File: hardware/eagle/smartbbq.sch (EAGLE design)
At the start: 58 parts, among them J1 MJ_2523_SMT, J2 MJ_2523_SMT, J3 MJ_2523_SMT, J4 MJ_2523_SMT, J5 5.5od/2.1id, J6 5.5od/2.5id, J7 5.5od/2.5id, J8 22-05-7028-02, J9 22-05-7028-02, P1 CMT_1603_SMT, Q1 SSM6N58NU, U2 TLV1117-50IDCY

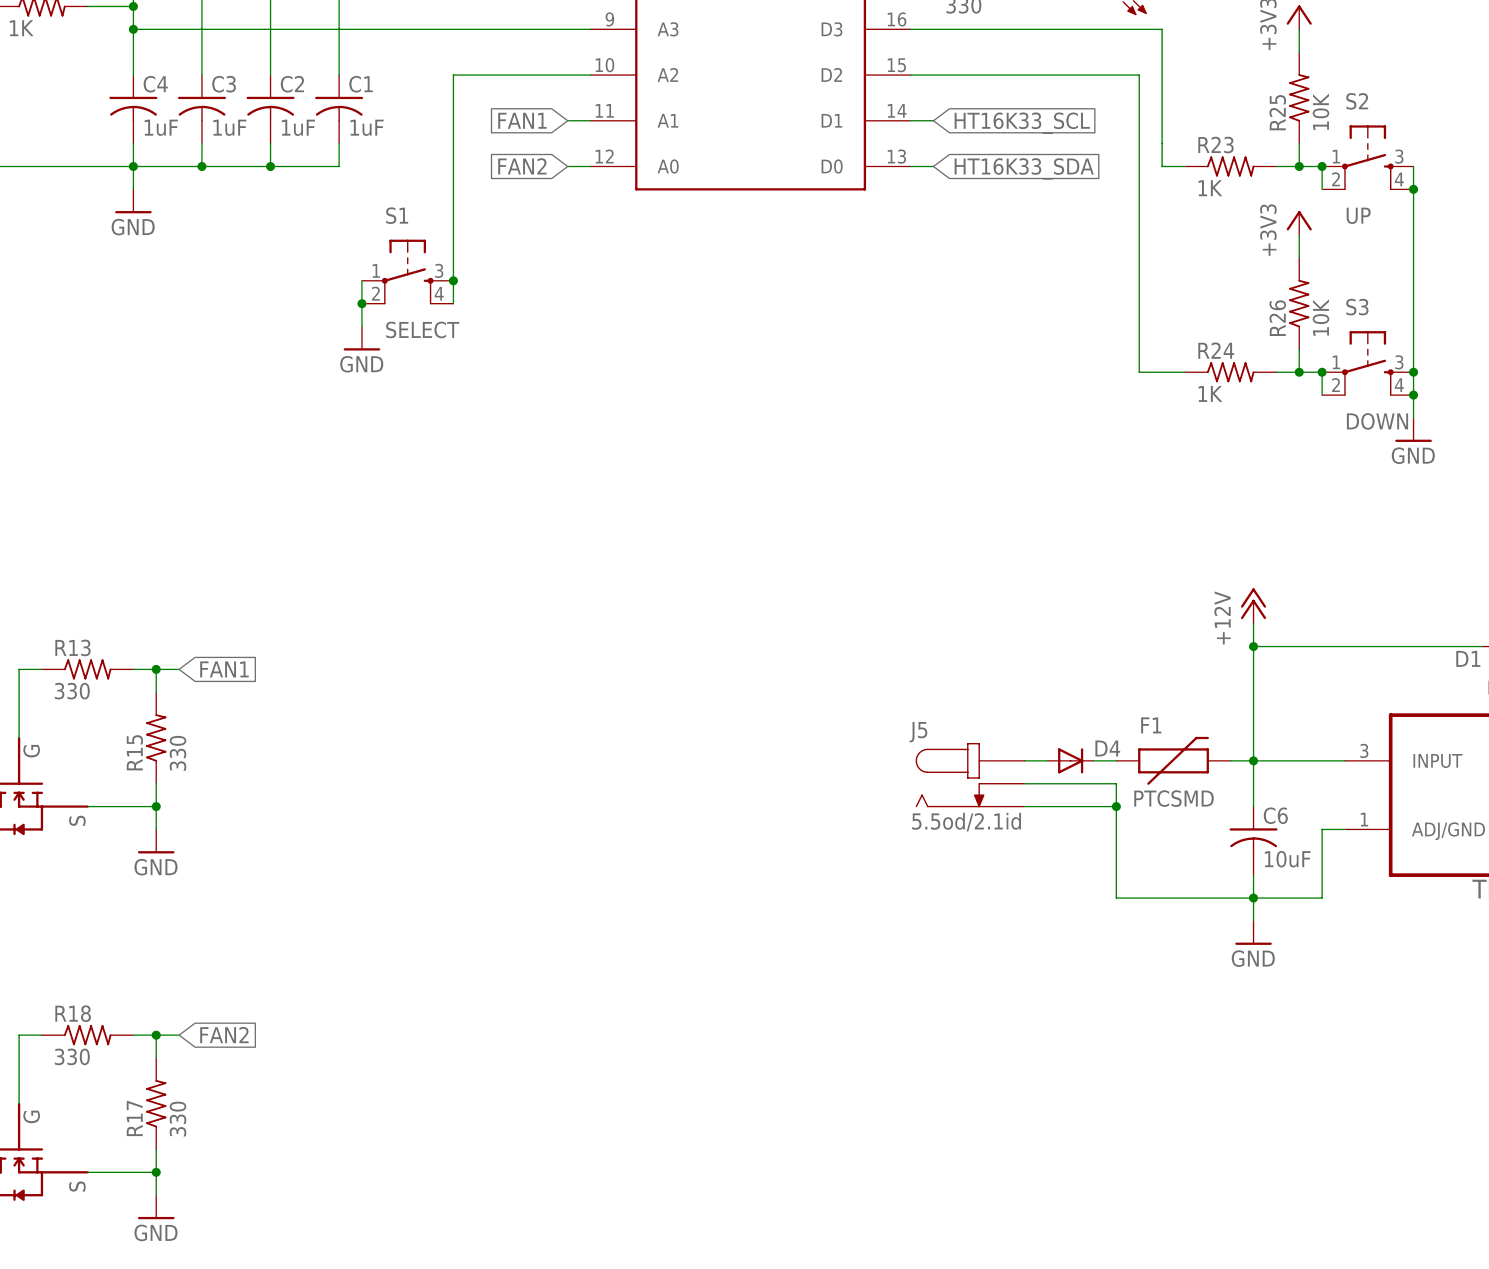
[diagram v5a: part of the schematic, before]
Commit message: Added resistors and tweaked values
Added missing select switch resistors and changed probe input resistor
values.
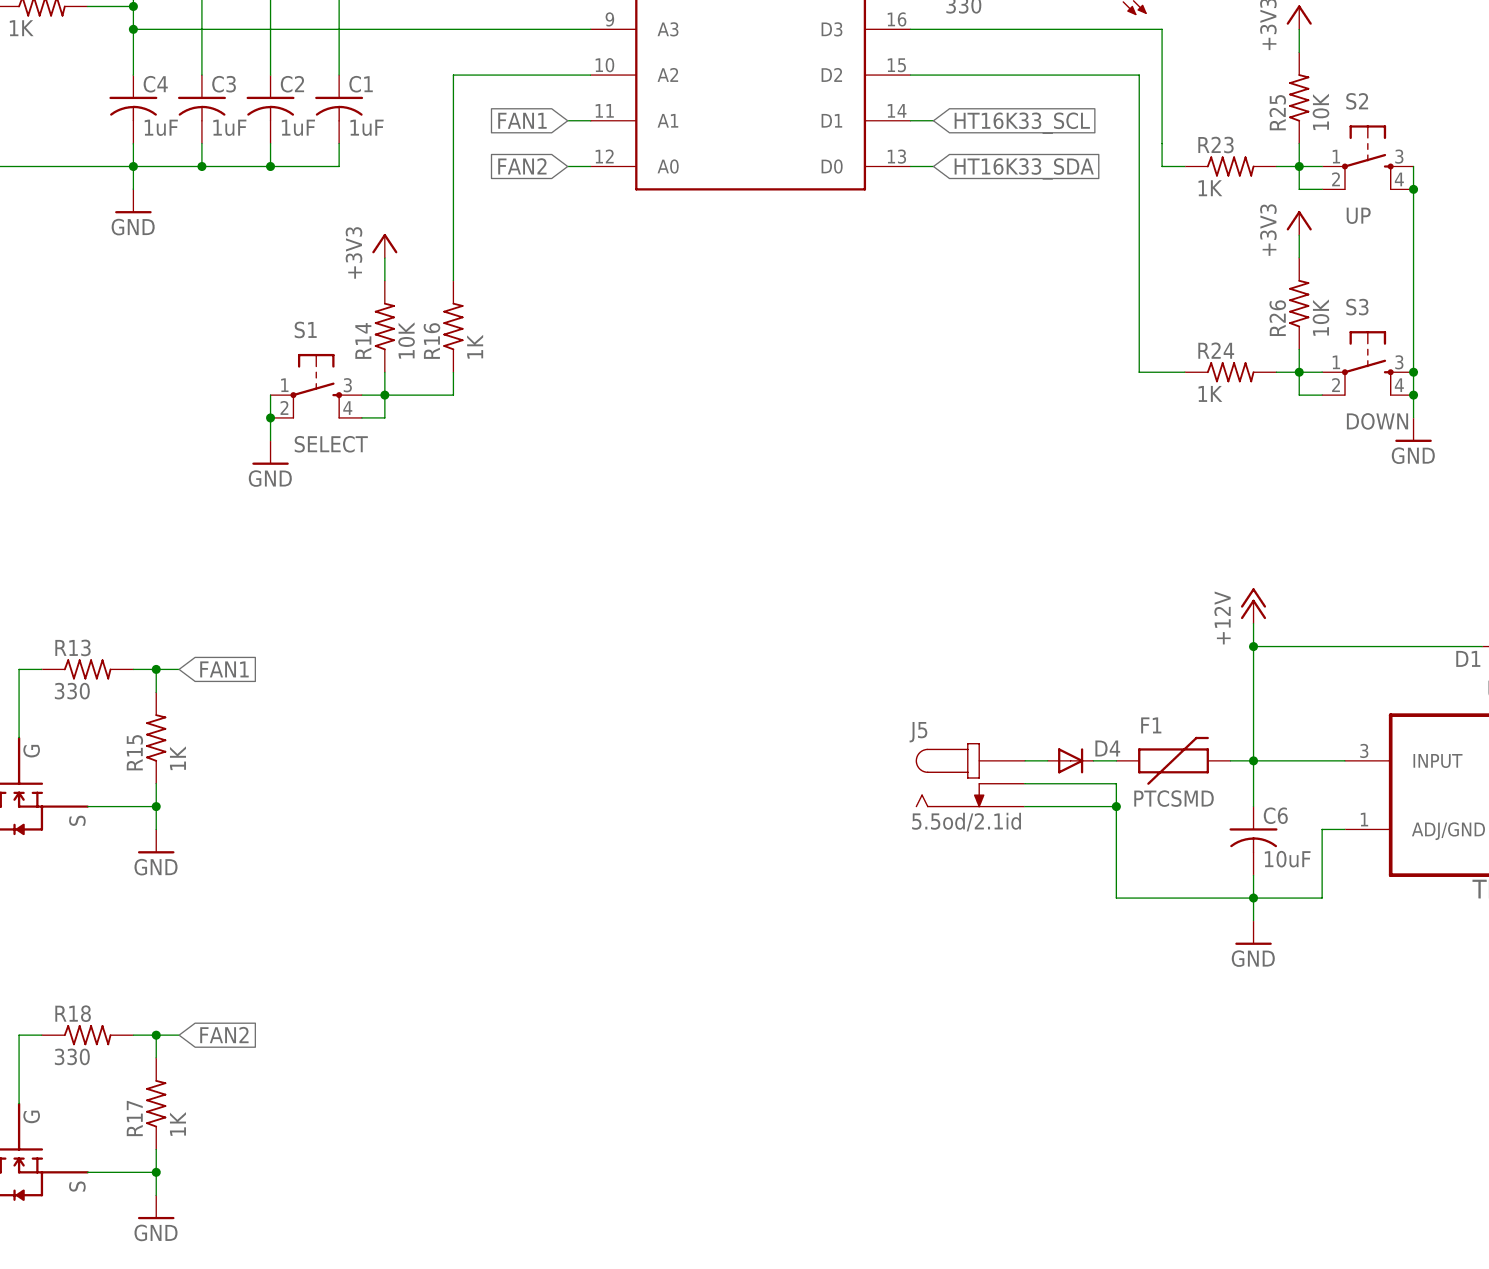
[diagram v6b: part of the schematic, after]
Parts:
- added R14: 10K, rcl:R-US_R0805
- added R16: 1K, rcl:R-US_R0805
- R15, R17: value 330 -> 1K
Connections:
- new net N$35: R14.1, R16.1, S1.3, S1.4
- net +3V3: now also R14.2
- net N$16: now also R16.2; no longer S1.3, S1.4
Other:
- moved on the sheet: S1
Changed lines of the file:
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@@
 <part name="J5" library="engirati" deviceset="PJ_002AH_SMT" device="" value="5.5od/2.1id"/>
 <part name="J6" library="engirati" deviceset="PJ_002AH_SMT" device="" value="5.5od/2.5id"/>
-<part name="R15" library="rcl" deviceset="R-US_" device="R0805" value="330"/>
+<part name="R15" library="rcl" deviceset="R-US_" device="R0805" value="1K"/>
 <part name="J8" library="con-molex" deviceset="22-?-02" device="05-7028" value=""/>
 <part name="Q1" library="engirati" deviceset="SSM6N58NU" device=""/>
@@
 <part name="J7" library="engirati" deviceset="PJ_002AH_SMT" device="" value="5.5od/2.5id"/>
 <part name="J9" library="con-molex" deviceset="22-?-02" device="05-7028" value=""/>
-<part name="R17" library="rcl" deviceset="R-US_" device="R0805" value="330"/>
+<part name="R17" library="rcl" deviceset="R-US_" device="R0805" value="1K"/>
 <part name="R18" library="rcl" deviceset="R-US_" device="R0805" value="330"/>
 <part name="GND10" library="SparkFun" deviceset="GND" device=""/>
@@
 <part name="D4" library="engirati" deviceset="FAIRCHILD_S1A_SMT" device="" value=""/>
 <part name="F1" library="SparkFun-PowerIC" deviceset="PTC" device="SMD"/>
+<part name="+3V5" library="supply1" deviceset="+3V3" device=""/>
+<part name="R14" library="rcl" deviceset="R-US_" device="R0805" value="10K"/>
+<part name="R16" library="rcl" deviceset="R-US_" device="R0805" value="1K"/>
 </parts>
 <sheets>
@@
 <instance part="LED_USR2" gate="G$1" x="195.58" y="160.02" rot="R90"/>
 <instance part="LED_USR3" gate="G$1" x="190.5" y="154.94" rot="R90"/>
-<instance part="S1" gate="S" x="111.76" y="121.92"/>
+<instance part="S1" gate="S" x="101.6" y="109.22"/>
 <instance part="S2" gate="S" x="218.44" y="134.62"/>
 <instance part="S3" gate="S" x="218.44" y="111.76"/>
 <instance part="GND1" gate="1" x="223.52" y="104.14"/>
-<instance part="GND2" gate="1" x="106.68" y="114.3"/>
+<instance part="GND2" gate="1" x="96.52" y="101.6"/>
 <instance part="FRAME1" gate="G$1" x="0" y="0"/>
 <instance part="FRAME1" gate="G$2" x="172.72" y="0"/>
@@
 <instance part="D4" gate="G$1" x="187.96" y="68.58"/>
 <instance part="F1" gate="G$1" x="195.58" y="68.58"/>
+<instance part="+3V5" gate="G$1" x="109.22" y="127"/>
+<instance part="R14" gate="G$1" x="109.22" y="116.84" rot="R90"/>
+<instance part="R16" gate="G$1" x="116.84" y="116.84" rot="R90"/>
 </instances>
 <busses>
@@
 <pinref part="GND2" gate="1" pin="GND"/>
 <pinref part="S1" gate="S" pin="2"/>
-<wire x1="106.68" y1="116.84" x2="106.68" y2="119.38" width="0.1524" layer="91"/>
+<wire x1="96.52" y1="104.14" x2="96.52" y2="106.68" width="0.1524" layer="91"/>
 <pinref part="S1" gate="S" pin="1"/>
-<wire x1="106.68" y1="119.38" x2="106.68" y2="121.92" width="0.1524" layer="91"/>
-<junction x="106.68" y="119.38"/>
+<wire x1="96.52" y1="106.68" x2="96.52" y2="109.22" width="0.1524" layer="91"/>
+<junction x="96.52" y="106.68"/>
 </segment>
 <segment>
@@
 <net name="N$16" class="0">
 <segment>
-<pinref part="S1" gate="S" pin="4"/>
-<pinref part="S1" gate="S" pin="3"/>
-<wire x1="116.84" y1="119.38" x2="116.84" y2="121.92" width="0.1524" layer="91"/>
 <pinref part="SPARK" gate="G$1" pin="A2"/>
 <wire x1="132.08" y1="144.78" x2="116.84" y2="144.78" width="0.1524" layer="91"/>
+<pinref part="R16" gate="G$1" pin="2"/>
 <wire x1="116.84" y1="121.92" x2="116.84" y2="144.78" width="0.1524" layer="91"/>
-<junction x="116.84" y="121.92"/>
 </segment>
 </net>
@@
 <wire x1="210.82" y1="127" x2="210.82" y2="124.46" width="0.1524" layer="91"/>
 </segment>
+<segment>
+<pinref part="+3V5" gate="G$1" pin="+3V3"/>
+<pinref part="R14" gate="G$1" pin="2"/>
+<wire x1="109.22" y1="124.46" x2="109.22" y2="121.92" width="0.1524" layer="91"/>
+</segment>
 </net>
 <net name="+12V" class="0">
@@
 <segment>
 <pinref part="S2" gate="S" pin="1"/>
-<pinref part="S2" gate="S" pin="2"/>
-<wire x1="213.36" y1="132.08" x2="213.36" y2="134.62" width="0.1524" layer="91"/>
 <pinref part="R23" gate="G$1" pin="2"/>
 <wire x1="208.28" y1="134.62" x2="210.82" y2="134.62" width="0.1524" layer="91"/>
-<junction x="213.36" y="134.62"/>
 <pinref part="R25" gate="G$1" pin="1"/>
 <wire x1="210.82" y1="134.62" x2="213.36" y2="134.62" width="0.1524" layer="91"/>
 <wire x1="210.82" y1="137.16" x2="210.82" y2="134.62" width="0.1524" layer="91"/>
 <junction x="210.82" y="134.62"/>
+<pinref part="S2" gate="S" pin="2"/>
+<wire x1="213.36" y1="132.08" x2="210.82" y2="132.08" width="0.1524" layer="91"/>
+<wire x1="210.82" y1="132.08" x2="210.82" y2="134.62" width="0.1524" layer="91"/>
 </segment>
 </net>
@@
 <wire x1="210.82" y1="111.76" x2="208.28" y2="111.76" width="0.1524" layer="91"/>
 <pinref part="S3" gate="S" pin="1"/>
-<pinref part="S3" gate="S" pin="2"/>
-<wire x1="213.36" y1="109.22" x2="213.36" y2="111.76" width="0.1524" layer="91"/>
 <wire x1="210.82" y1="111.76" x2="213.36" y2="111.76" width="0.1524" layer="91"/>
 <junction x="210.82" y="111.76"/>
-<junction x="213.36" y="111.76"/>
+<pinref part="S3" gate="S" pin="2"/>
+<wire x1="213.36" y1="109.22" x2="210.82" y2="109.22" width="0.1524" layer="91"/>
+<wire x1="210.82" y1="109.22" x2="210.82" y2="111.76" width="0.1524" layer="91"/>
 </segment>
 </net>
@@
 </segment>
 </net>
+<net name="N$35" class="0">
+<segment>
+<pinref part="S1" gate="S" pin="3"/>
+<wire x1="106.68" y1="109.22" x2="109.22" y2="109.22" width="0.1524" layer="91"/>
+<pinref part="R14" gate="G$1" pin="1"/>
+<wire x1="109.22" y1="109.22" x2="109.22" y2="111.76" width="0.1524" layer="91"/>
+<pinref part="S1" gate="S" pin="4"/>
+<wire x1="106.68" y1="106.68" x2="109.22" y2="106.68" width="0.1524" layer="91"/>
+<wire x1="109.22" y1="106.68" x2="109.22" y2="109.22" width="0.1524" layer="91"/>
+<junction x="109.22" y="109.22"/>
+<pinref part="R16" gate="G$1" pin="1"/>
+<wire x1="109.22" y1="109.22" x2="116.84" y2="109.22" width="0.1524" layer="91"/>
+<wire x1="116.84" y1="109.22" x2="116.84" y2="111.76" width="0.1524" layer="91"/>
+</segment>
+</net>

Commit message: PCB added
PCB added and a few schematic tweaks
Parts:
- removed LED_USR, LED_USR1, LED_USR2, LED_USR3: (no value), SparkFun:LED0603
- removed R11: 10K, rcl:R-US_R0805
- added LED2, LED3, LED4, LED5: (no value), led:LEDCHIPLED_0805
- F1: value PTCSMD -> 2920L300-15DR; device SparkFun-PowerIC:PTCSMD -> engirati:2920L300-15DR
- J8, J9: value 22-05-7028-02 -> +
- S1: value SELECT -> PANASONIC-EVQ; device Spark:TAC_SWITCHSMD -> engirati:PANASONIC-EVQ
- S2: value UP -> PANASONIC-EVQ; device Spark:TAC_SWITCHSMD -> engirati:PANASONIC-EVQ
- S3: value DOWN -> PANASONIC-EVQ; device Spark:TAC_SWITCHSMD -> engirati:PANASONIC-EVQ
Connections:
- removed net N$26: R11.2, SPARK.!RST
- net +12V: now also F1.P$2; no longer F1.2
- net +3V3: no longer R11.1
- net GND: now also LED2.C, LED3.C, LED4.C, LED5.C, S1.3, S1.4; no longer LED_USR.C, LED_USR1.C, LED_USR2.C, LED_USR3.C, S1.1, S1.2
- net N$10: now also LED3.A; no longer LED_USR1.A
- net N$11: now also LED4.A; no longer LED_USR2.A
- net N$12: now also LED5.A; no longer LED_USR3.A
- net N$33: now also F1.P$1; no longer F1.1
- net N$35: now also S1.1, S1.2; no longer S1.3, S1.4
- net N$9: now also LED2.A; no longer LED_USR.A
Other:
- note added: "DOWN"
- note added: "SELECT"
- note added: "UP"
- moved on the sheet: D4, F1, J5

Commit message: rev0.1 of board
rev0.1 of board and minor schematic edits
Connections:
- net +12V: now also J8-1.S, J9-1.S; no longer J8-2.S, J9-2.S
- net N$30: now also J9-2.S; no longer J9-1.S
- net N$32: now also J8-2.S; no longer J8-1.S
